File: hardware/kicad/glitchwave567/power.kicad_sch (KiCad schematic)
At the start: 42 parts, among them J5 DC_2.1mm, Q10 AO3401A, Q11 BCP56, U18 L78L09, U19 MP1584EN, U6 TL074

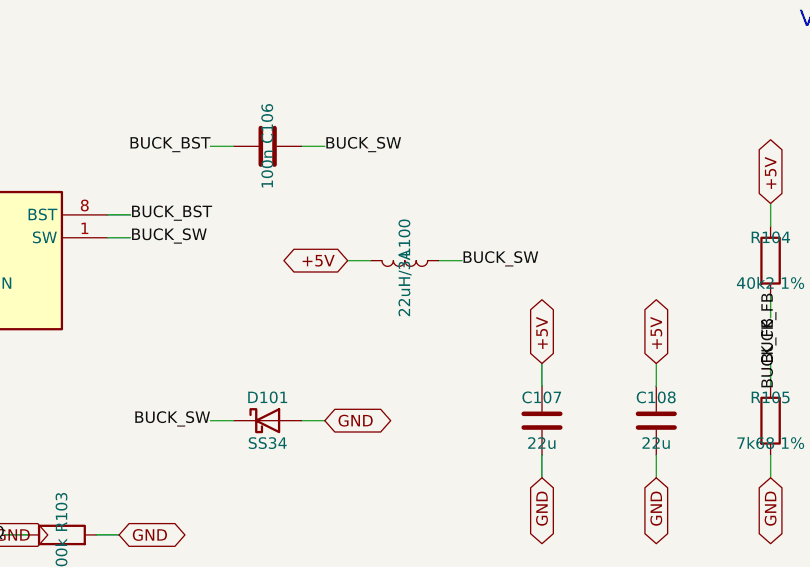
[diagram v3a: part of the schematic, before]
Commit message: hardware: turnkey BOM (319 parts, all semis verified vs live LCSC/JLC stock)
BOM.xlsx: MAIN 297 + CTRL 22 parts, grouped, LCSC C-numbers for every named
part. Highlights: LM13700MX/NOPB C174050 genuine TI x6 (5.7k stock);
MMBFJ201 C891687 genuine onsemi (EOL fear unfounded, 30k stock); LM567CMX
C18353; MP1584EN C15051 (NRND noted); CD4051/52 TI preferred-lib; Suntsu
stomps = Digi-Key line (Marketplace confirm flagged). Value fixes: 51k,
845R 1% Fetzer, inductor -> SMDRI127-220MT C9905 (12x12 fp). README sheet
carries first-article checklist.

Co-Authored-By: Claude Fable 5 <noreply@anthropic.com>
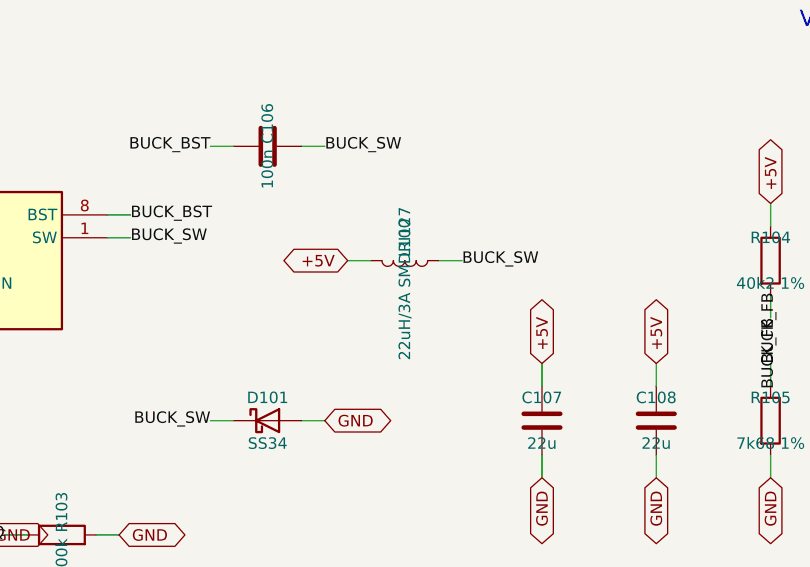
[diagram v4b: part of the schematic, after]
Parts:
- L100: value 22uH/3A -> 22uH/3A SMDRI127; footprint Inductor_SMD:L_Bourns-SRN8040_8x8.15mm -> Inductor_SMD:L_12x12mm_H8mm
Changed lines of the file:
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@@
       (effects (font (size 1.27 1.27)))
     )
-    (property "Value" "22uH/3A" (id 1) (at 111.76 129.54 0)
+    (property "Value" "22uH/3A SMDRI127" (id 1) (at 111.76 129.54 0)
       (effects (font (size 1.27 1.27)))
     )
-    (property "Footprint" "Inductor_SMD:L_Bourns-SRN8040_8x8.15mm" (id 2) (at 111.76 127.0 0)
+    (property "Footprint" "Inductor_SMD:L_12x12mm_H8mm" (id 2) (at 111.76 127.0 0)
       (effects (font (size 1.27 1.27)) hide)
     )

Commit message: hardware: fix C107 duplicate refdes, add missing courtyards, rename silkscreen
Pre-order verification pass before sending the boards to PCBWay. Full write-up in
hardware/fab/ORDER_READINESS_20260911.md.

C107 was a duplicate reference designator: a 100n 0603 on FREQ_CV in mcu.kicad_sch
and a 22uF 0805 in power.kicad_sch that is the MP1584's second output capacitor.
Only the 100n existed on the PCB, so the +5V rail (Pico plus six WS2812B via J10)
would have been built with half its intended bulk capacitance, and the BOM listed
C107 twice with conflicting parts. KiCad collapses a duplicate refdes to one
component, so footprint count matched symbol count, DRC schematic parity passed and
ERC said nothing. Only a designator-level BOM-vs-board-vs-CPL diff finds it.

  - power.kicad_sch: the 22uF symbol renamed C107 to C112
  - MAIN PCB: C112 placed at (62.6, 25.0), 0.3mm F.Cu stub to the +5V trunk at
    y=23.65, GND through the F.Cu pour exactly as C108 is connected. Placement
    chosen by a clearance search, nearest obstacle 0.42mm against a 0.13mm rule.
    No via: every via position in that pocket scored under 0.23mm against the
    In2.Cu diagonals. Zones refilled.
  - BOM.xlsx: the 22uF row's designators changed from C107,C108 to C108,C112

Courtyards added to the 13 footprints that had none (J1-J6 and U20 on MAIN,
RV1-RV6 on CONTROL), copied from the library footprints. DRC was structurally blind
to body collisions on exactly the largest mechanical parts, which is why both jack
collisions went undetected in July. Every footprint on both boards now has one.
That exposed two more courtyard overlaps on MAIN, both courtyard-only with the
bodies clear: J5 to FB100 (0.700mm of body air, ~0.21mm of copper) and J4 to R98
(0.338mm). Nothing was moved because nothing collides.

Silkscreen on both boards renamed from "GLITCHWAVE 567" to "WHERE THE FUZZ MEETS
THE FUNK". Font 1.2 to 1.0mm so the longer string keeps about the same width:
measured in the plotted gerber it spans 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
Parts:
- C100: footprint Capacitor_SMD:CP_Elec_8x10.2 -> Capacitor_SMD:CP_Elec_8x10
- renumbered C107 to C112
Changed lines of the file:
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@@
       (effects (font (size 1.27 1.27)))
     )
-    (property "Footprint" "Capacitor_SMD:CP_Elec_8x10.2" (id 2) (at 109.22 66.04 0)
+    (property "Footprint" "Capacitor_SMD:CP_Elec_8x10" (id 2) (at 109.22 66.04 0)
       (effects (font (size 1.27 1.27)) hide)
     )
@@
   (symbol (lib_id "Device:C") (at 127.0 144.78 0) (unit 1)
     (in_bom yes) (on_board yes) (dnp no)
-    (property "Reference" "C107" (id 0) (at 127.0 142.24 0)
+    (property "Reference" "C112" (id 0) (at 127.0 142.24 0)
       (effects (font (size 1.27 1.27)))
     )
@@
       (project "glitchwave567"
         (path "/"
-          (reference "C107") (unit 1)
-        )
-      )
+          (reference "C112") (unit 1)
+        )
+      )
